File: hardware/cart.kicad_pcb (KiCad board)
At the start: 2 copper layers, 83.7 x 42 mm, 34 parts, among them J3 jumper-bridged, J4 debug-snoop, P1 edge connector, U1 74LVC138, U2 1.5A @ 3.3V, U3 74LVC8T245, U4 74LVC8T245, U5 74LVC8T245, U6 S29AL016J55TFIR20, U7 74LVC8T245, U8 74LVC8T245

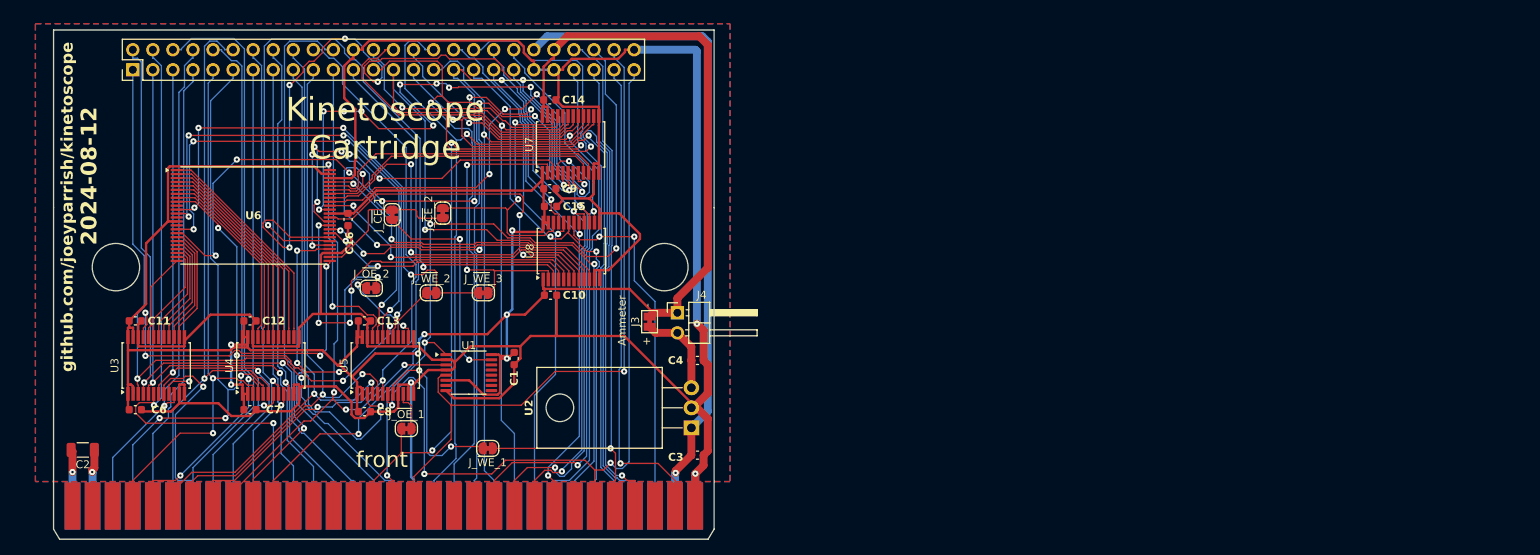
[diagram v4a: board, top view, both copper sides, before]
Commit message: Streamline cart board
 - Let JLCPCB populate the base header
 - Switch regulator for SMD version that JLCPCB can populate
 - Move components for easier routing, easier access to ammeter header
 - Add explanatory text in the silkscreen for each section of the PCB
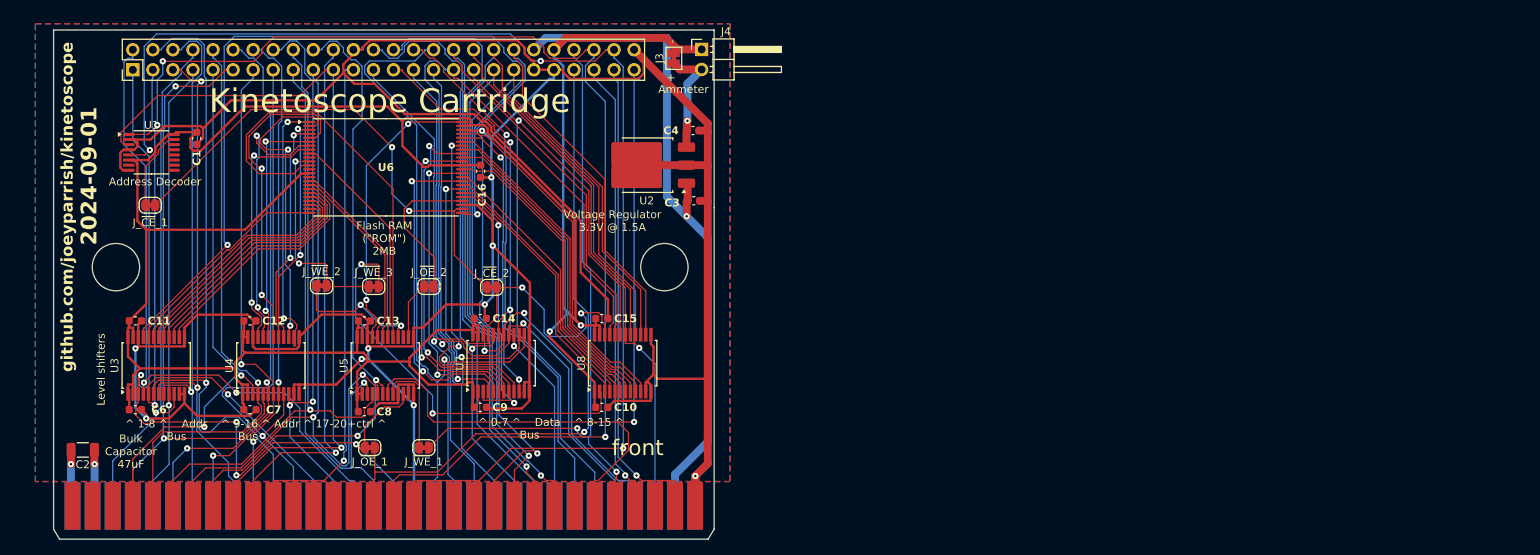
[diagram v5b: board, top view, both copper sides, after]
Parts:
- J3, J_~{CE}_1, J_~{CE}_2, J_~{OE}_1, J_~{OE}_2, J_~{WE}_1, J_~{WE}_2, J_~{WE}_3: value jumper-bridged -> (none)
- U1: value 74LVC138 -> 74LVC138A
- U2: value 1.5A @ 3.3V -> MCP1827S-3302E/EB; footprint Package_TO_SOT_THT:TO-220-3_Horizontal_TabDown -> Package_TO_SOT_SMD:TO-252-3_TabPin2
- moved C1 48.9 mm to (31.1, 27.2)
- moved U1 48.9 mm to (25.4, 29.0)
- moved U2 33.8 mm to (88.1, 30.6), turned to 180 degrees
- moved J3 33.5 mm to (91.6, 17.1)
- moved J4 33.5 mm to (95.1, 16.0)
- moved C3 32.2 mm to (94.1, 35.1)
- moved J_~{CE}_1 30.7 mm to (25.2, 35.7), turned to 0 degrees
- moved C4 29.1 mm to (94.0, 26.2)
- moved U7 29.1 mm to (69.7, 55.7)
- moved C14 29.1 mm to (67.1, 50.0)
- moved C9 29.1 mm to (67.1, 61.3)
- moved U6 17.9 mm to (55.1, 30.9)
- moved C16 17.9 mm to (67.1, 31.4)
- moved U8 15.6 mm to (85.1, 55.7)
- moved C10 15.6 mm to (82.5, 61.3)
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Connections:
- net Net-(J3-A) renamed /+3.3V_INT
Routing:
- net GND: track 389.3 -> 469.1 mm, vias 3 -> 10
- net /~{SEGA_AS}: track 85.0 -> 161.4 mm, vias 1 -> 3
- net /flash-internal/D1_3V: track 106.0 -> 31.9 mm, vias 6 -> 2
- net /flash-internal/A0_3V: track 44.0 -> 105.1 mm, vias 4 -> 2
- net /~{SEGA_CE}: track 93.8 -> 153.6 mm, vias 4 -> 3
- net /flash-internal/D8_3V: track 92.8 -> 33.4 mm, vias 2 -> 0
- net /flash-internal/~{CE_3V_INT}: track 19.1 -> 64.2 mm, vias 0 -> 2
- net /SEGA_D9: track 67.5 -> 107.4 mm, vias 1 -> 0
- net /SEGA_D12: track 63.4 -> 102.4 mm, vias 2 -> 1
- net /flash-internal/~{WE_3V_INT}: track 64.6 -> 26.4 mm, vias 4 -> 2
- net /SEGA_D15: track 74.1 -> 111.5 mm, vias 2 -> 1
- net /flash-internal/A18_3V: track 61.7 -> 24.5 mm, vias 4 -> 0
- net /SEGA_D13: track 69.5 -> 106.4 mm, vias 2 -> 1
- net /flash-internal/A17_3V: track 59.0 -> 24.0 mm, vias 4 -> 0
- net /SEGA_D2: track 106.4 -> 72.2 mm
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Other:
- board text added: "2024-09-01"
- board text added: "Address Decoder"
- board text added: "Bulk Capacitor 47uF"
- board text added: "Flash RAM ({dblquote}ROM{dblquote}) 2MB"
- board text added: "Level shifters"
- board text added: "Voltage Regulator 3.3V @ 1.5A"
- board text added: "^ 0-7 ^ Data ^ 8-15 ^ Bus"
- board text added: "^ 1-8 ^ Addr ^ 9-16 ^ Addr ^ 17-20+ctrl ^ Bus Bus"
- board text removed: "2024-08-12"

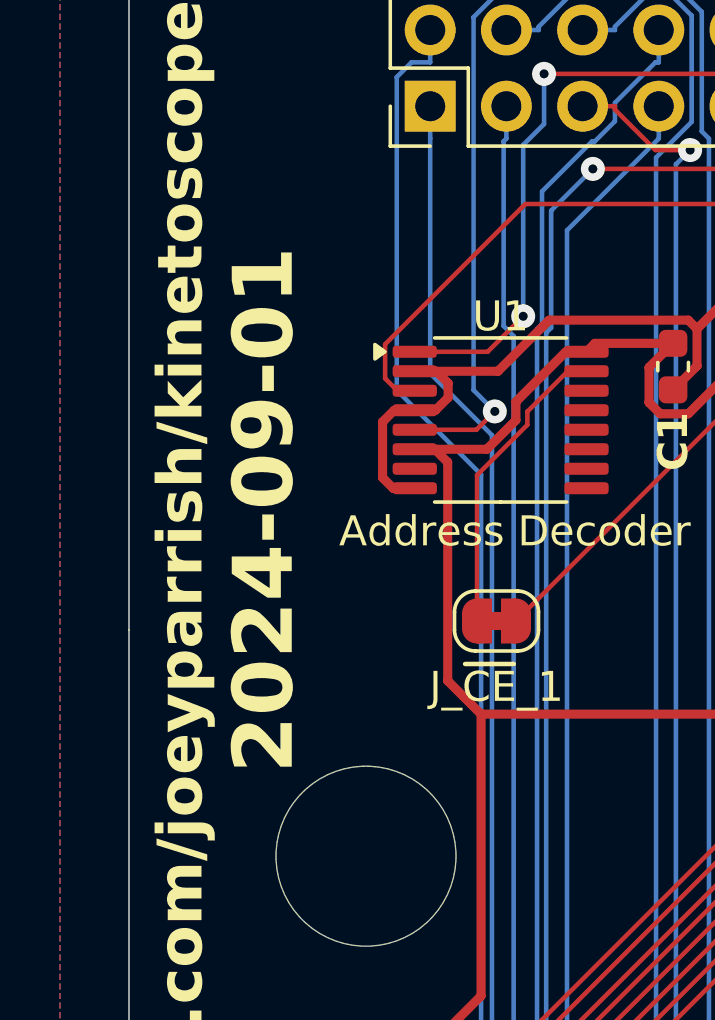
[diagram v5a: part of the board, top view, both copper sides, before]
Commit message: Fix rotation of SMD voltage regulator
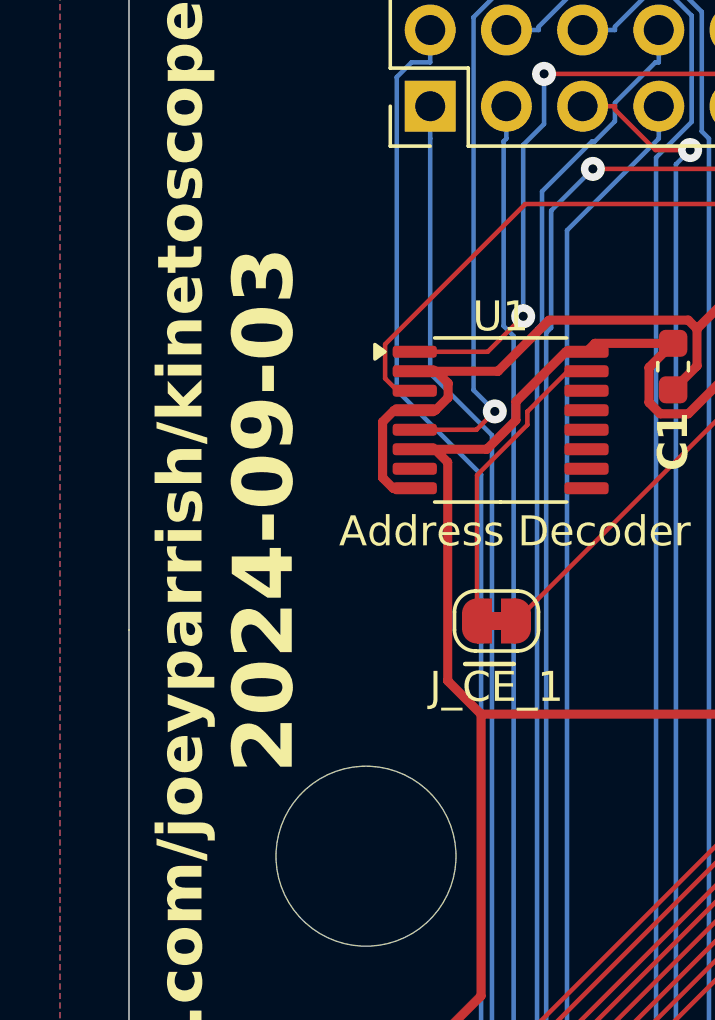
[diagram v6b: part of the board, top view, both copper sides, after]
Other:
- board text added: "2024-09-03"
- board text removed: "2024-09-01"
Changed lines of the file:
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@@
 		)
 	)
-	(gr_text "2024-09-01"
+	(gr_text "2024-09-03"
 		(at 17.5 32 90)
 		(layer "F.SilkS")
@@
 			)
 		)
-		(render_cache "2024-09-01" 90
+		(render_cache "2024-09-03" 90
 			(polygon
 				(pts
@@
 			(polygon
 				(pts
-					(xy 16.329162 24.563293) (xy 16.329162 24.307327) (xy 18.085757 24.307327) (xy 18.085757 23.800767)
-					(xy 18.33 23.800767) (xy 18.33 25.08353) (xy 18.085757 25.08353) (xy 18.085757 24.574528) (xy 16.703831 24.574528)
-					(xy 17.054075 24.912072) (xy 16.843538 25.049825)
+					(xy 16.329162 25.086461) (xy 16.329162 23.797836) (xy 16.598318 23.797836) (xy 17.142002 24.33517)
+					(xy 17.142002 24.101674) (xy 17.616322 23.797836) (xy 18.071591 23.797836) (xy 18.33 24.045498)
+					(xy 18.33 25.086461) (xy 18.085757 25.086461) (xy 18.085757 24.152477) (xy 17.996852 24.062107)
+					(xy 17.65247 24.062107) (xy 17.386245 24.245289) (xy 17.386245 24.659036) (xy 17.131256 24.659036)
+					(xy 16.573405 24.109978) (xy 16.573405 25.086461)
 				)
 			)

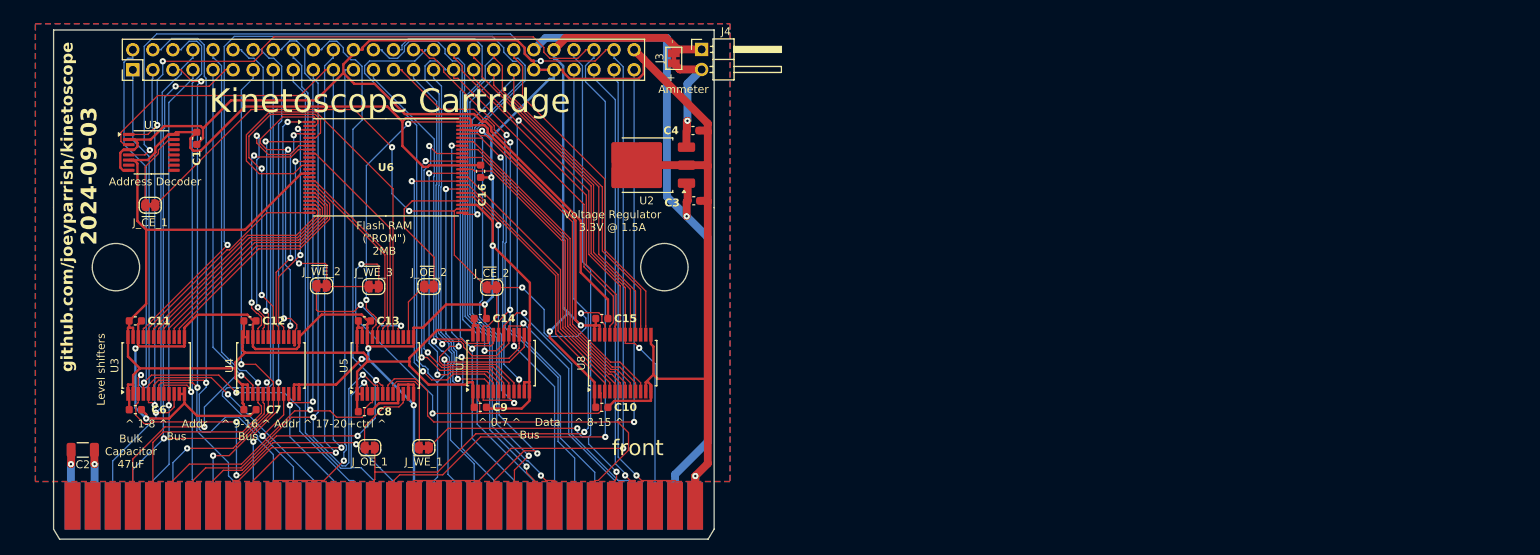
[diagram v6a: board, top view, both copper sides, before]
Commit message: Fix footprint for new SMD regulator
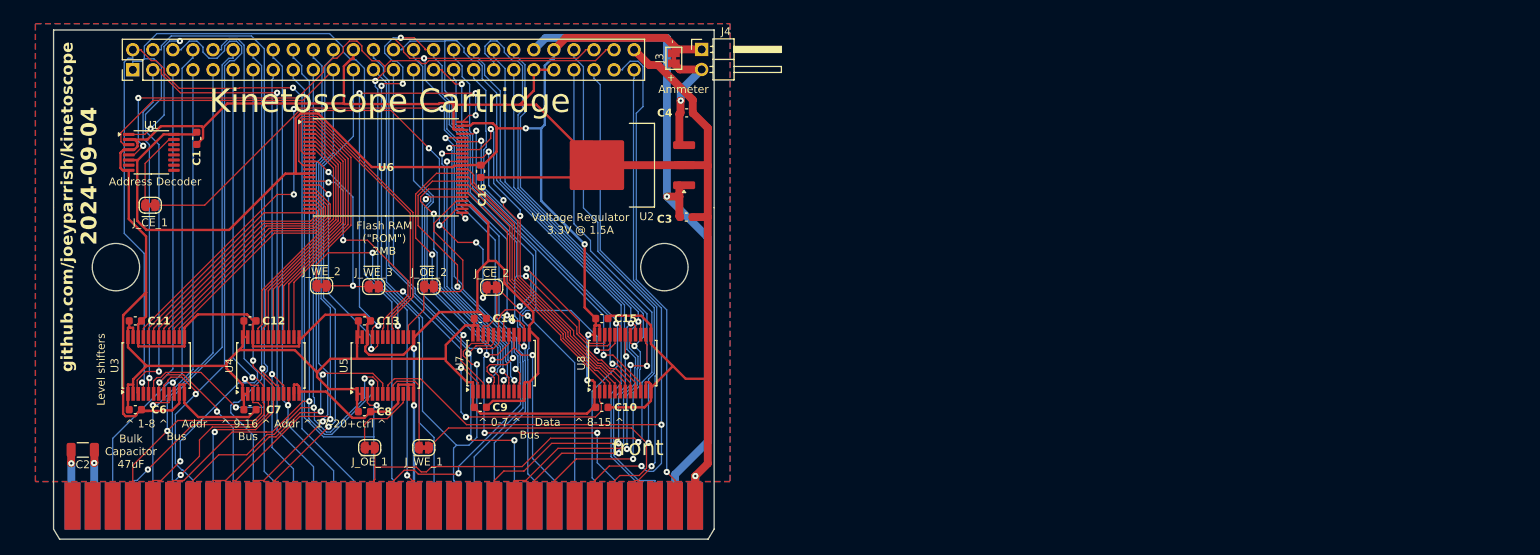
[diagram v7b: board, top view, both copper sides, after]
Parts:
- moved C4 2.38 mm to (93.2, 24.0)
- moved C3 2.27 mm to (93.2, 37.2)
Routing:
- net +3.3V: track 329.3 -> 284.5 mm, vias 2 -> 4
- net /SEGA_A1: track 95.9 -> 139.7 mm, vias 4 -> 1
- net /SEGA_A2: track 83.2 -> 124.5 mm
- net /SEGA_A3: track 75.8 -> 113.4 mm
- net /flash-internal/A0_3V: track 105.1 -> 72.9 mm, vias 2 -> 4
- net /SEGA_D13: track 106.4 -> 77.1 mm, vias 1 -> 2
- net /SEGA_D7: track 85.4 -> 114.1 mm, vias 1 -> 4
- net /SEGA_D9: track 107.4 -> 79.1 mm, vias 0 -> 1
- net /SEGA_D10: track 94.4 -> 66.3 mm
- net /~{SEGA_AS}: track 161.4 -> 133.8 mm, vias 3 -> 4
- net GND: track 469.1 -> 442.0 mm, vias 10 -> 3
- net /SEGA_D8: track 105.4 -> 78.9 mm, vias 0 -> 1
- net /SEGA_D15: track 111.5 -> 85.4 mm, vias 1 -> 3
- net /SEGA_D3: track 92.8 -> 118.9 mm, vias 2 -> 1
- net /SEGA_D14: track 101.4 -> 77.1 mm, vias 1 -> 2
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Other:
- board text added: "2024-09-04"
- board text removed: "2024-09-03"

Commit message: Replace 8-bit buffers with cheaper version
Replace SN74LVC8T245DBR (8-bit buffers) with SN74LVC8T245PWR.  The old
version was SSOP, and the new version is a TSSOP size, but they are
otherwise the same.

This is estimated to reduce the price of a complete unit by over $11,
or about 16.5%.
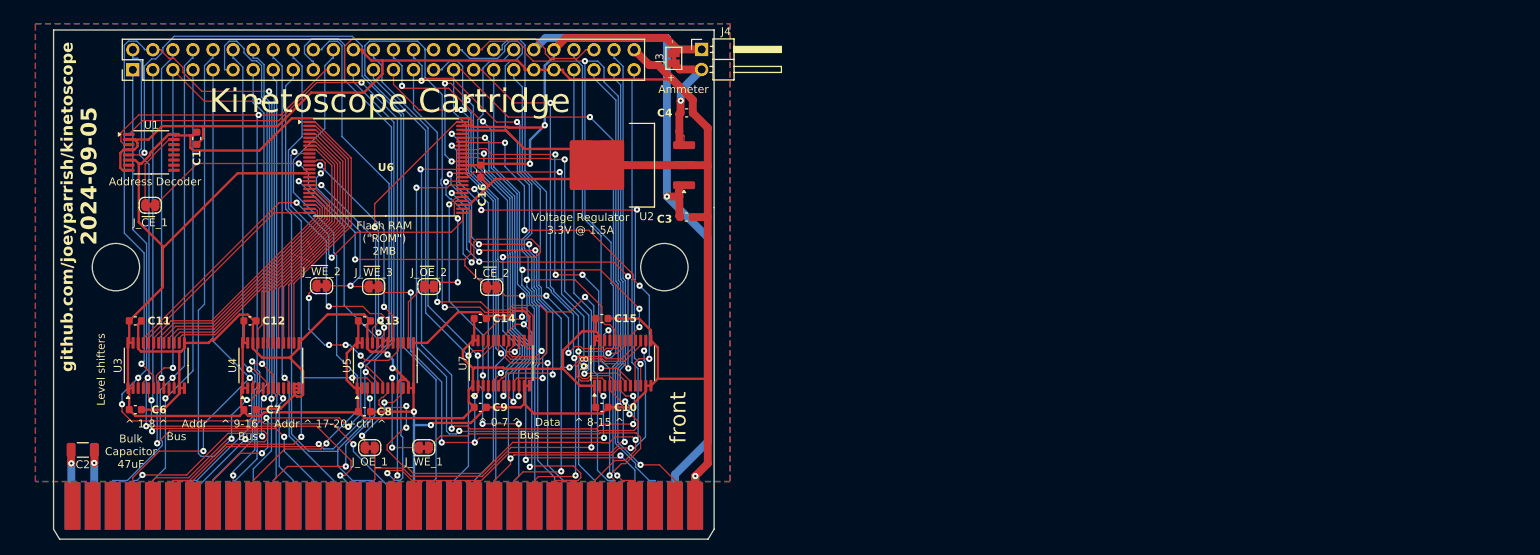
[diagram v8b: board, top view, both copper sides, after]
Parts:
- J3, J_~{CE}_1, J_~{CE}_2, J_~{OE}_1, J_~{OE}_2, J_~{WE}_1, J_~{WE}_2, J_~{WE}_3: value (none) -> ~
- U3, U4, U5, U7, U8: footprint Package_SO:SSOP-24_5.3x8.2mm_P0.65mm -> Package_SO:TSSOP-24_4.4x7.8mm_P0.65mm
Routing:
- net /~{SEGA_AS}: track 133.8 -> 189.2 mm, vias 4 -> 3
- net /SEGA_A1: track 139.7 -> 87.6 mm, vias 1 -> 3
- net /SEGA_D11: track 73.0 -> 119.9 mm, vias 1 -> 2
- net /SEGA_A5: track 64.5 -> 108.1 mm
- net /SEGA_A2: track 124.5 -> 85.8 mm, vias 2 -> 3
- net /SEGA_A3: track 113.4 -> 75.2 mm, vias 2 -> 3
- net /SEGA_D8: track 78.9 -> 116.2 mm, vias 1 -> 2
- net /flash-internal/D9_3V: track 34.5 -> 70.3 mm, vias 0 -> 4
- net GND: track 442.0 -> 407.8 mm, vias 3 -> 5
- net /SEGA_D3: track 118.9 -> 86.4 mm, vias 1 -> 5
- net /flash-internal/D11_3V: track 37.3 -> 69.5 mm, vias 0 -> 4
- net /SEGA_A4: track 92.5 -> 120.1 mm, vias 1 -> 2
- net /flash-internal/D4_3V: track 34.5 -> 58.0 mm, vias 2 -> 4
- net /flash-internal/D8_3V: track 33.1 -> 56.0 mm, vias 0 -> 4
- net /flash-internal/A16_3V: track 52.0 -> 33.8 mm, vias 4 -> 2
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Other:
- board text added: "2024-09-05"
- board text removed: "2024-09-04"
